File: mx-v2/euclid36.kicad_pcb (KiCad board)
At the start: 2 copper layers, 248.2 x 127 mm, 112 parts, among them SW1 RotaryEncoder_Switch, SW10 SW_PUSH, SW11 SW_PUSH, SW12 SW_PUSH, SW14 SW_PUSH, SW15 SW_PUSH, SW16 SW_PUSH, SW17 SW_PUSH, SW18 SW_PUSH, SW19 SW_PUSH, SW2 SW_PUSH, SW20 SW_PUSH, SW21 SW_PUSH, SW22 SW_PUSH, SW23 SW_PUSH, SW25 SW_PUSH, SW26 SW_PUSH, SW27 SW_PUSH, SW28 SW_PUSH, SW29 SW_PUSH, SW3 SW_PUSH, SW31 SW_PUSH, SW32 SW_PUSH, SW33 SW_PUSH, SW34 SW_PUSH, SW35 SW_PUSH, SW37 SW_PUSH, SW38 SW_PUSH, SW39 SW_PUSH, SW4 SW_PUSH, SW40 SW_PUSH, SW41 SW_PUSH, SW42 SW_PUSH, SW5 SW_PUSH, SW6 SW_PUSH, SW7 RotaryEncoder_Switch, SW8 SW_PUSH, SW9 SW_PUSH, U1 USBLC6-2SC6, U2 ATmega32U4-AU, Y1 XTAL

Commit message: updated with drill holes for spacers
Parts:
- added Ref**: Val**, _reviung-kbd:spacer_m2, F.Cu at (168.1, 43.1)
- added Ref**: Val**, _reviung-kbd:spacer_m2, F.Cu at (51.2, 94.8)
- added Ref**: Val**, _reviung-kbd:spacer_m2, F.Cu at (132.0, 42.8)
- added Ref**: Val**, _reviung-kbd:spacer_m2, F.Cu at (248.7, 31.2)
- added Ref**: Val**, _reviung-kbd:spacer_m2, F.Cu at (54.6, 31.6)
- added Ref**: Val**, _reviung-kbd:spacer_m2, F.Cu at (109.5, 79.8)
- added Ref**: Val**, _reviung-kbd:spacer_m2, F.Cu at (191.6, 80.8)
- added Ref**: Val**, _reviung-kbd:spacer_m2, F.Cu at (252.1, 93.8)
- added Ref**: Val**, _reviung-kbd:spacer_m2, F.Cu at (197.9, 112.2)
- added Ref**: Val**, _reviung-kbd:spacer_m2, F.Cu at (103.2, 112.4)

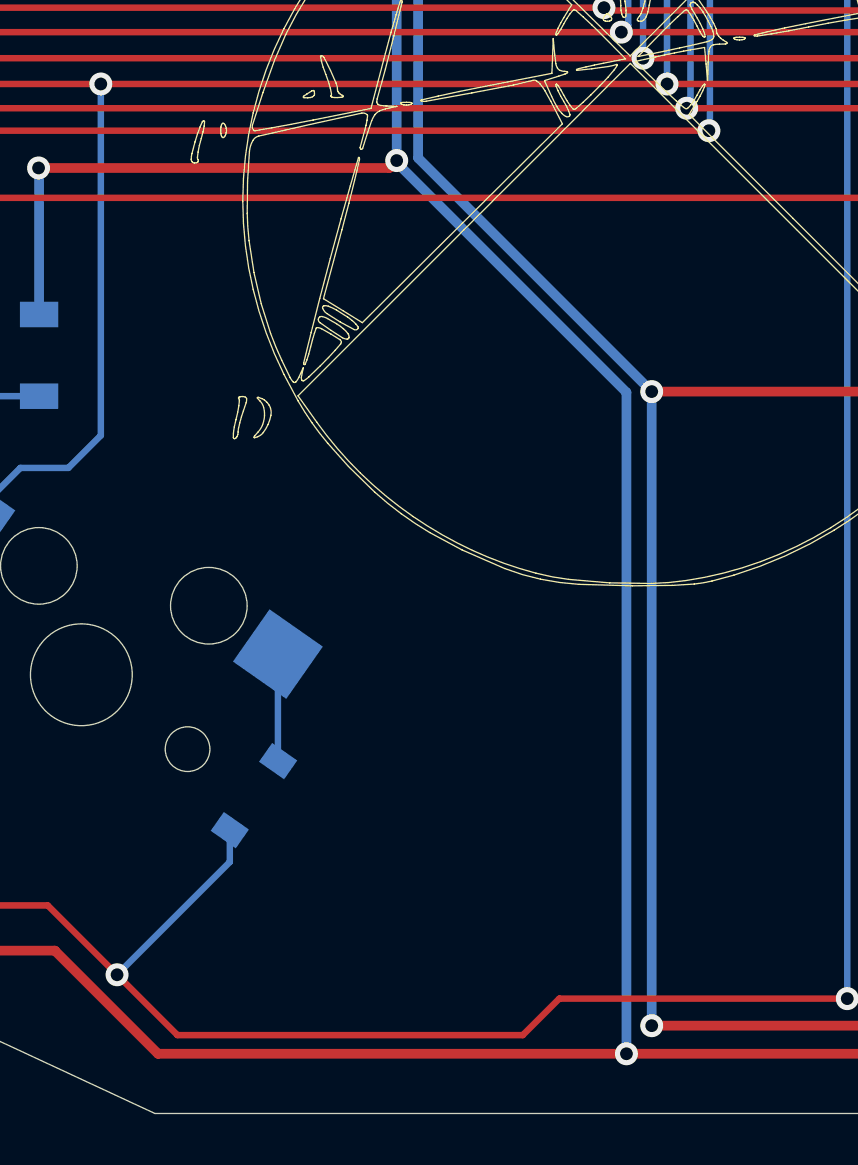
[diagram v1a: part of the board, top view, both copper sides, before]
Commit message: Added one more spacer hole for top and bottom plates
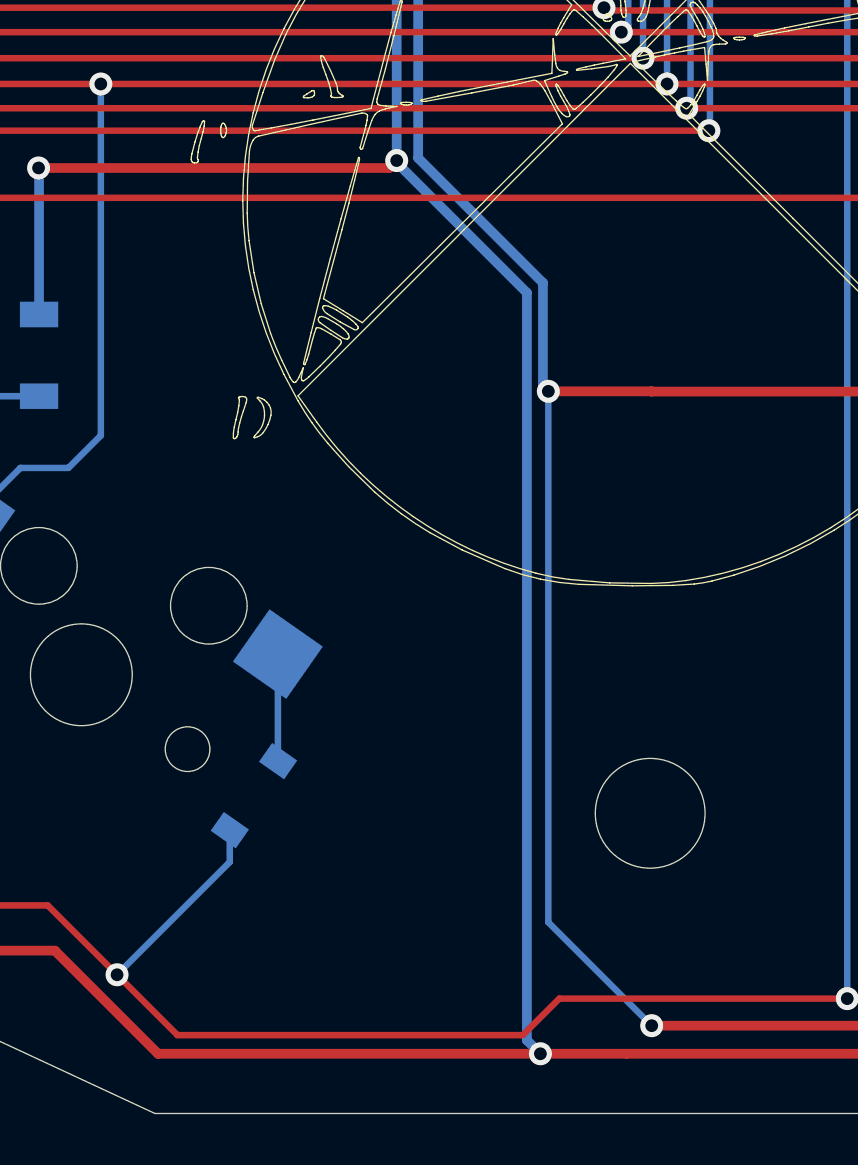
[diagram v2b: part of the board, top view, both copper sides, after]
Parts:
- added Ref**: Val**, _reviung-kbd:spacer_m2, F.Cu at (151.5, 140.6)
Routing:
- net VCC: track 887.7 -> 891.7 mm
- net GND: track 1139.2 -> 1137.8 mm
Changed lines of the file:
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@@
     (thickness 1.6)
     (drawings 2733)
-    (tracks 1530)
+    (tracks 1537)
     (zones 0)
-    (modules 122)
+    (modules 123)
     (nets 98)
   )
@@
   )
   (module _reviung-kbd:spacer_m2 (layer F.Cu)
+    (at 151.48 140.64)
+    (descr "Mounting Hole 2.2mm, no annular, M2")
+    (tags "mounting hole 2.2mm no annular m2")
+    (attr virtual)
+    (fp_text reference Ref** (at -0.95 -0.55) (layer F.Fab) hide
+      (effects (font (size 1 1) (thickness 0.15)))
+    )
+    (fp_text value Val** (at 0 0.55) (layer F.Fab) hide
+      (effects (font (size 1 1) (thickness 0.15)))
+    )
+    (pad "" np_thru_hole circle (at 0 0) (size 4.3 4.3) (drill 4.3) (layers *.Cu *.Mask))
+  )
+  (module _reviung-kbd:spacer_m2 (layer F.Cu)
     (at 168.14 43.07)
     (descr "Mounting Hole 2.2mm, no annular, M2")
@@
   (segment (start 142.13101 84.719338) (end 142.390501 84.978829) (width 0.381) (layer B.Cu) (net 44))
   (via (at 151.54 148.96) (size 0.9) (drill 0.5) (layers F.Cu B.Cu) (net 44))
-  (segment (start 151.54 124.12) (end 151.54 148.96) (width 0.381) (layer B.Cu) (net 44))
-  (segment (start 142.390501 114.970501) (end 151.54 124.12) (width 0.381) (layer B.Cu) (net 44))
   (segment (start 151.54 148.96) (end 168.77 148.96) (width 0.381) (layer F.Cu) (net 44))
   (segment (start 168.77 148.96) (end 174.96 142.77) (width 0.381) (layer F.Cu) (net 44))
@@
   (segment (start 171.34 123.55) (end 171.33 123.56) (width 0.381) (layer B.Cu) (net 44))
   (segment (start 173.46 123.55) (end 171.34 123.55) (width 0.381) (layer B.Cu) (net 44))
-  (via (at 151.54 124.12) (size 0.9) (drill 0.5) (layers F.Cu B.Cu) (net 44))
   (segment (start 170.77 124.12) (end 151.54 124.12) (width 0.381) (layer F.Cu) (net 44))
   (segment (start 171.33 123.56) (end 170.77 124.12) (width 0.381) (layer F.Cu) (net 44))
@@
   (segment (start 181.15 27.92) (end 181.18 27.95) (width 0.381) (layer F.Cu) (net 44))
   (segment (start 171.09 27.92) (end 181.15 27.92) (width 0.381) (layer F.Cu) (net 44))
+  (segment (start 147.28 123.8995) (end 147.4905 124.11) (width 0.381) (layer B.Cu) (net 44))
+  (segment (start 147.28 119.86) (end 147.28 123.8995) (width 0.381) (layer B.Cu) (net 44))
+  (via (at 147.4905 124.11) (size 0.9) (drill 0.5) (layers F.Cu B.Cu) (net 44))
+  (segment (start 142.390501 114.970501) (end 147.28 119.86) (width 0.381) (layer B.Cu) (net 44))
+  (segment (start 151.53 124.11) (end 151.54 124.12) (width 0.381) (layer F.Cu) (net 44))
+  (segment (start 147.4905 124.11) (end 151.53 124.11) (width 0.381) (layer F.Cu) (net 44))
+  (segment (start 147.4905 144.9105) (end 151.54 148.96) (width 0.254) (layer B.Cu) (net 44))
+  (segment (start 147.4905 124.11) (end 147.4905 144.9105) (width 0.254) (layer B.Cu) (net 44))
   (segment (start 130.9375 27.42) (end 128.5125 29.845) (width 0.381) (layer F.Cu) (net 45))
   (segment (start 139.24 27.42) (end 130.9375 27.42) (width 0.381) (layer F.Cu) (net 45))
@@
   (segment (start 139.24 27.42) (end 139.24 27.42) (width 0.381) (layer F.Cu) (net 45))
   (via (at 139.24 27.42) (size 0.9) (drill 0.5) (layers F.Cu B.Cu) (net 45))
-  (via (at 150.55 150.06) (size 0.9) (drill 0.5) (layers F.Cu B.Cu) (net 45))
-  (segment (start 150.55 124.15) (end 150.55 150.06) (width 0.381) (layer B.Cu) (net 45))
   (segment (start 150.55 150.06) (end 168.82 150.06) (width 0.381) (layer F.Cu) (net 45))
-  (segment (start 141.55 115.15) (end 150.55 124.15) (width 0.381) (layer B.Cu) (net 45))
-  (segment (start 132.2 150.06) (end 150.55 150.06) (width 0.381) (layer F.Cu) (net 45))
   (via (at 256.69 68.38) (size 0.9) (drill 0.5) (layers F.Cu B.Cu) (net 45))
   (segment (start 256.64 68.43) (end 256.69 68.38) (width 0.381) (layer B.Cu) (net 45))
@@
   (segment (start 156.17 73.93) (end 156.14 73.9) (width 0.381) (layer F.Cu) (net 45))
   (segment (start 161.73 73.93) (end 156.17 73.93) (width 0.381) (layer F.Cu) (net 45))
+  (via (at 147.18 150.06) (size 0.9) (drill 0.5) (layers F.Cu B.Cu) (net 45))
+  (segment (start 146.65 149.53) (end 147.18 150.06) (width 0.381) (layer B.Cu) (net 45))
+  (segment (start 146.65 120.25) (end 146.65 149.53) (width 0.381) (layer B.Cu) (net 45))
+  (segment (start 147.18 150.06) (end 150.55 150.06) (width 0.381) (layer F.Cu) (net 45))
+  (segment (start 132.2 150.06) (end 147.18 150.06) (width 0.381) (layer F.Cu) (net 45))
+  (segment (start 141.55 115.15) (end 146.65 120.25) (width 0.381) (layer B.Cu) (net 45))
   (via (at 153.78 113.9) (size 0.9) (drill 0.5) (layers F.Cu B.Cu) (net 46))
   (segment (start 153.82 113.86) (end 153.78 113.9) (width 0.254) (layer B.Cu) (net 46))
